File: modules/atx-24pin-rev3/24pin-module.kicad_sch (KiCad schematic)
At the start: 82 parts, among them J1 TO-HUB, J2 TO-HUB-PWR, J3 ATX-24 PSU, J5 USB-C 2.0, J6 TO-HUB-STACK, SW1 BOOT, SW2 RESET, U1 ESP32-C6-MINI-1-N4, U10 INA238, U11 INA238, U12 INA238, U13 INA238, U2 TJA1051T/3, U3 LP5907MFX-3.3, U5 TPS2121RUXR, U612V1 INA181A2IDBVR, U63V31 INA181A2IDBVR, U65V1 INA181A2IDBVR, U65VSB1 INA181A2IDBVR, U712V1 TLV7011DBVR, U73V31 TLV7011DBVR, U75V1 TLV7011DBVR, U75VSB1 TLV7011DBVR

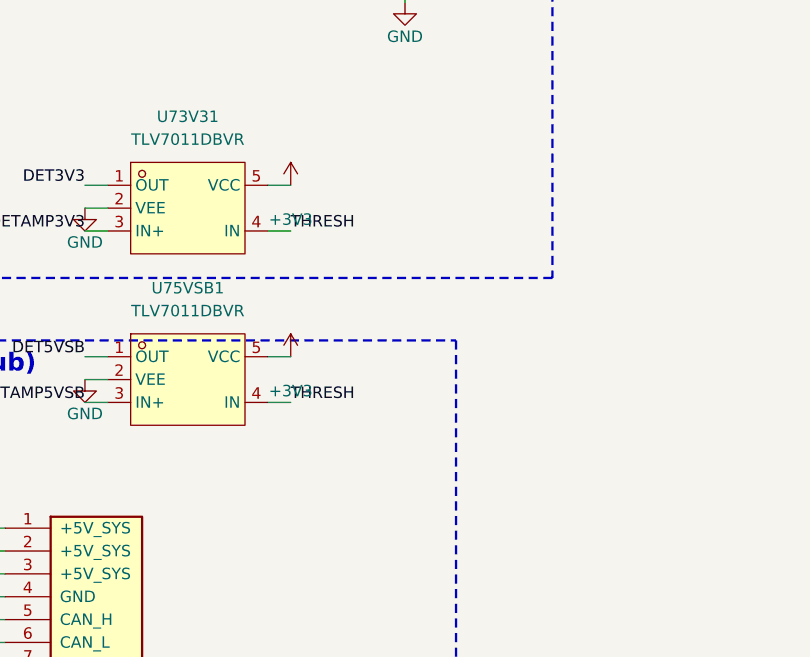
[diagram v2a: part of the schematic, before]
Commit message: 24-pin: add comparator bypass caps C73V31/C75VSB1 to the new 3V3/5VSB cells
The decoupler sweep found the two new detection cells were missing the TLV7011
comparator VCC bypass (the existing 12V/5V cells each carry TWO caps: C6<rail>1
amp + C7<rail>1 comparator). Added C73V31 (3V3) + C75VSB1 (5VSB), 100nF +3V3->GND,
mirroring C712V1/C75V1. All four cells now symmetric (8 bypass caps total).

Co-Authored-By: Claude Opus 4.8 <noreply@anthropic.com>
Claude-Session: https://claude.ai/code/session_01LvfqcnEeuin2oyJQw548EX
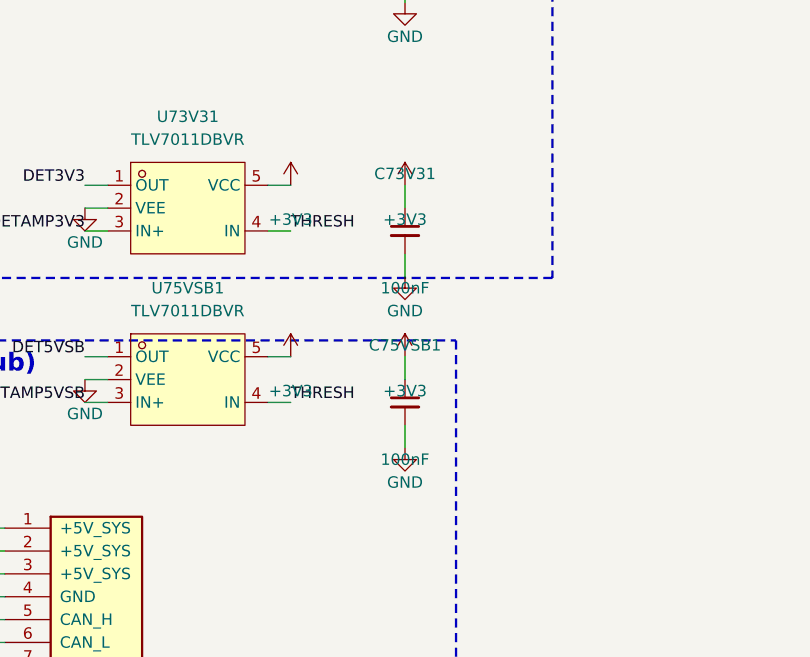
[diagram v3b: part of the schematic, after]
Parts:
- added C73V31, C75VSB1: 100nF, cec-Capacitor_SMD:C_0402_1005Metric, symbol cec-vendor:C_Small
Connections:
- net +3V3: now also C73V31.1, C75VSB1.1
- net GND: now also C73V31.2, C75VSB1.2
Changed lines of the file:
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@@
 		(stroke (width 0) (type default)))
 	(label "GPIO0" (at 78.74 306.07 270) (effects (font (size 1.27 1.27)) (justify left bottom)))
+	(symbol
+		(lib_id "cec-vendor:C_Small")
+		(at 388.62 144.78 0)
+		(unit 1)
+		(exclude_from_sim no)
+		(in_bom yes)
+		(on_board yes)
+		(dnp no)
+		(fields_autoplaced yes)
+		(property "Reference" "C73V31" (at 388.62 138.43 0) (effects (font (size 1.27 1.27))))
+		(property "Value" "100nF" (at 388.62 151.13 0) (effects (font (size 1.27 1.27))))
+		(property "Footprint" "cec-Capacitor_SMD:C_0402_1005Metric" (at 388.62 144.78 0) (effects (font (size 1.27 1.27)) (hide yes)))
+		(property "Datasheet" "" (at 388.62 144.78 0) (effects (font (size 1.27 1.27)) (hide yes)))
+		(pin "1")
+		(pin "2")
+		(instances
+			(project "24pin-module"
+				(path "/a4774022-41d4-4be7-85b6-fed5477a3f9f" (reference "C73V31") (unit 1))
+			)
+		)
+	)
+	(wire (pts (xy 388.62 142.24) (xy 388.62 139.7))
+		(stroke (width 0) (type default)))
+	(symbol
+		(lib_id "cec-power:+3V3")
+		(at 388.62 139.7 0)
+		(unit 1)
+		(exclude_from_sim no)
+		(in_bom yes)
+		(on_board yes)
+		(dnp no)
+		(property "Reference" "#PWR0940" (at 388.62 137.16 0) (effects (font (size 1.27 1.27)) (hide yes)))
+		(property "Value" "+3V3" (at 388.62 143.51 0) (effects (font (size 1.27 1.27))))
+		(pin "1")
+		(instances
+			(project "24pin-module"
+				(path "/a4774022-41d4-4be7-85b6-fed5477a3f9f" (reference "#PWR0940") (unit 1))
+			)
+		)
+	)
+	(wire (pts (xy 388.62 147.32) (xy 388.62 149.86))
+		(stroke (width 0) (type default)))
+	(symbol
+		(lib_id "cec-power:GND")
+		(at 388.62 149.86 0)
+		(unit 1)
+		(exclude_from_sim no)
+		(in_bom yes)
+		(on_board yes)
+		(dnp no)
+		(property "Reference" "#PWR0941" (at 388.62 147.32 0) (effects (font (size 1.27 1.27)) (hide yes)))
+		(property "Value" "GND" (at 388.62 153.67 0) (effects (font (size 1.27 1.27))))
+		(pin "1")
+		(instances
+			(project "24pin-module"
+				(path "/a4774022-41d4-4be7-85b6-fed5477a3f9f" (reference "#PWR0941") (unit 1))
+			)
+		)
+	)
+	(symbol
+		(lib_id "cec-vendor:C_Small")
+		(at 388.62 163.83 0)
+		(unit 1)
+		(exclude_from_sim no)
+		(in_bom yes)
+		(on_board yes)
+		(dnp no)
+		(fields_autoplaced yes)
+		(property "Reference" "C75VSB1" (at 388.62 157.48 0) (effects (font (size 1.27 1.27))))
+		(property "Value" "100nF" (at 388.62 170.18 0) (effects (font (size 1.27 1.27))))
+		(property "Footprint" "cec-Capacitor_SMD:C_0402_1005Metric" (at 388.62 163.83 0) (effects (font (size 1.27 1.27)) (hide yes)))
+		(property "Datasheet" "" (at 388.62 163.83 0) (effects (font (size 1.27 1.27)) (hide yes)))
+		(pin "1")
+		(pin "2")
+		(instances
+			(project "24pin-module"
+				(path "/a4774022-41d4-4be7-85b6-fed5477a3f9f" (reference "C75VSB1") (unit 1))
+			)
+		)
+	)
+	(wire (pts (xy 388.62 161.29) (xy 388.62 158.75))
+		(stroke (width 0) (type default)))
+	(symbol
+		(lib_id "cec-power:+3V3")
+		(at 388.62 158.75 0)
+		(unit 1)
+		(exclude_from_sim no)
+		(in_bom yes)
+		(on_board yes)
+		(dnp no)
+		(property "Reference" "#PWR0942" (at 388.62 156.21 0) (effects (font (size 1.27 1.27)) (hide yes)))
+		(property "Value" "+3V3" (at 388.62 162.56 0) (effects (font (size 1.27 1.27))))
+		(pin "1")
+		(instances
+			(project "24pin-module"
+				(path "/a4774022-41d4-4be7-85b6-fed5477a3f9f" (reference "#PWR0942") (unit 1))
+			)
+		)
+	)
+	(wire (pts (xy 388.62 166.37) (xy 388.62 168.91))
+		(stroke (width 0) (type default)))
+	(symbol
+		(lib_id "cec-power:GND")
+		(at 388.62 168.91 0)
+		(unit 1)
+		(exclude_from_sim no)
+		(in_bom yes)
+		(on_board yes)
+		(dnp no)
+		(property "Reference" "#PWR0943" (at 388.62 166.37 0) (effects (font (size 1.27 1.27)) (hide yes)))
+		(property "Value" "GND" (at 388.62 172.72 0) (effects (font (size 1.27 1.27))))
+		(pin "1")
+		(instances
+			(project "24pin-module"
+				(path "/a4774022-41d4-4be7-85b6-fed5477a3f9f" (reference "#PWR0943") (unit 1))
+			)
+		)
+	)
 	(sheet_instances
 		(path "/"
